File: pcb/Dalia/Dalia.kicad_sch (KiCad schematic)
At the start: 3 parts

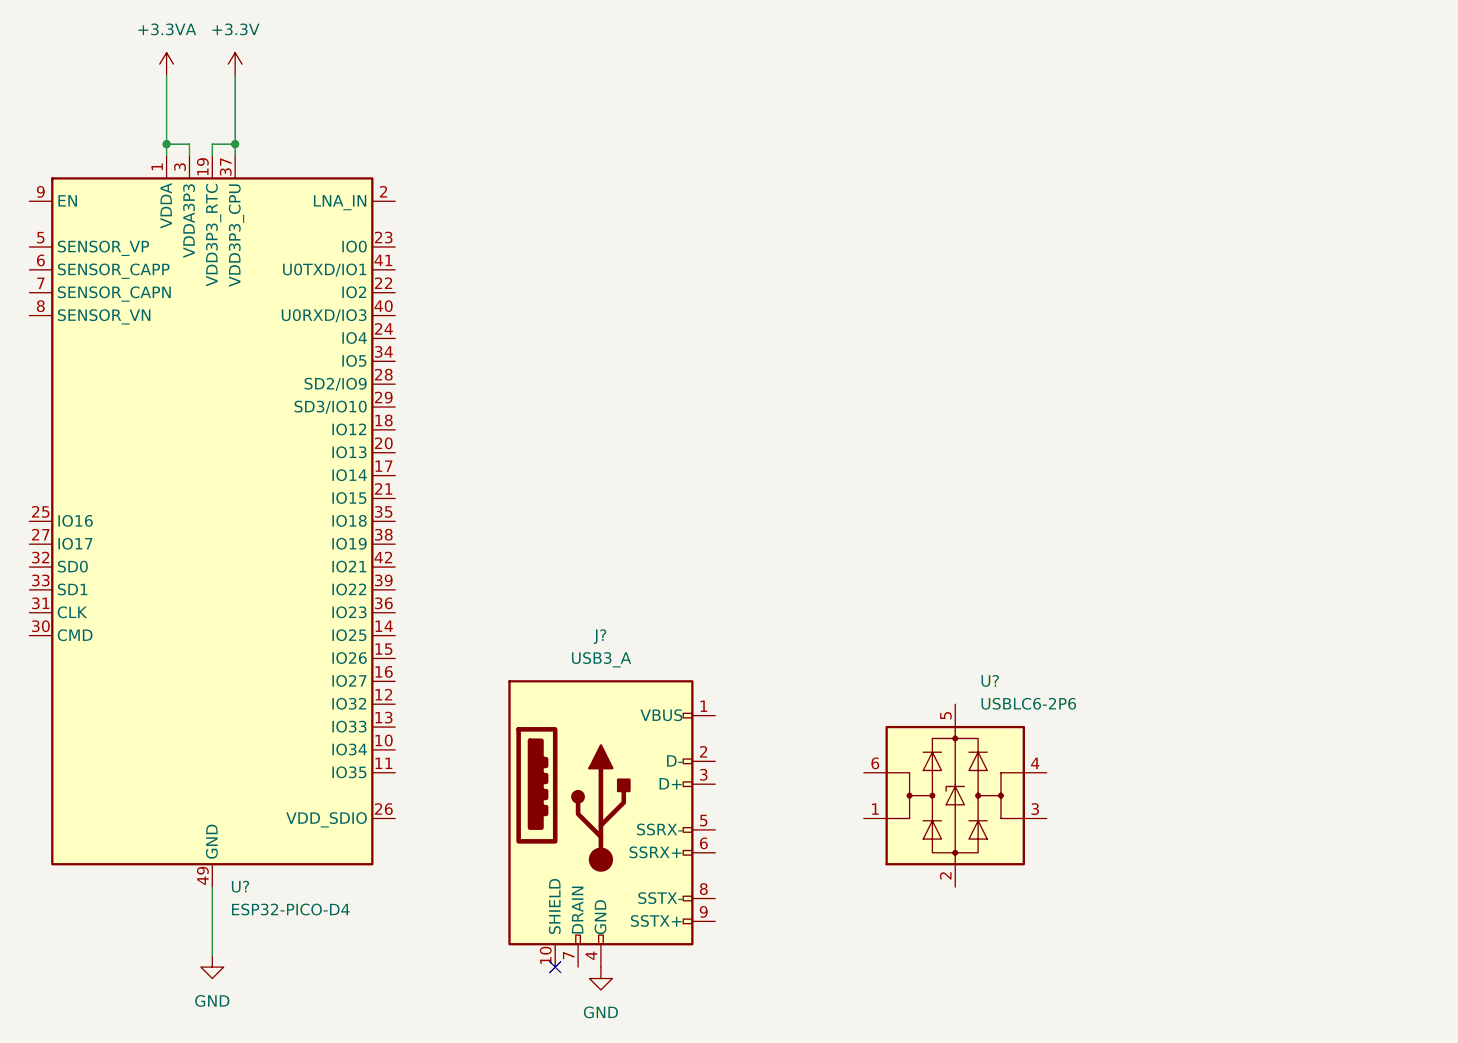
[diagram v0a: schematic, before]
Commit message: Changed PCB layout
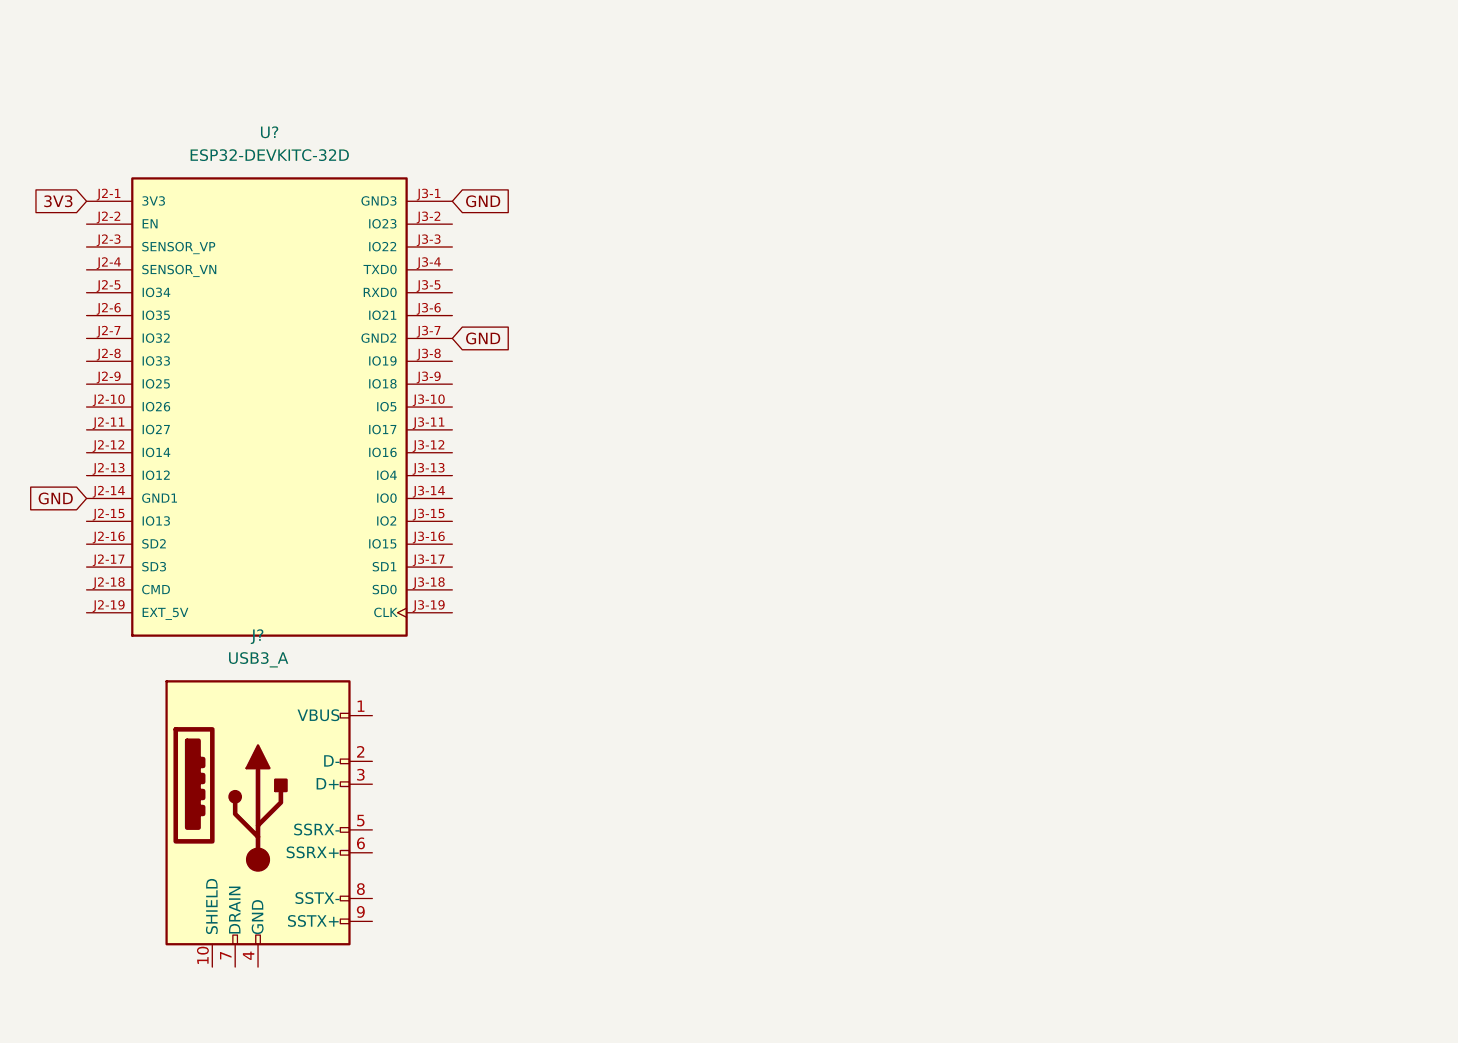
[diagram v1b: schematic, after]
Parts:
- removed U?: USBLC6-2P6, Package_TO_SOT_SMD:SOT-666, symbol Power_Protection:USBLC6-2P6
- removed U?: ESP32-PICO-D4, Package_DFN_QFN:QFN-48-1EP_7x7mm_P0.5mm_EP5.3x5.3mm, symbol RF_Module:ESP32-PICO-D4
- added U?: ESP32-DEVKITC-32D, MODULE_ESP32-DEVKITC-32D, symbol ESP32-DEVKITC-32D:ESP32-DEVKITC-32D
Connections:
- net GND: now also U?.J2-14 (GND1), U?.J3-1 (GND3), U?.J3-7 (GND2); no longer J?.4 (GND)
- new net 3V3: U?.J2-1 (3V3)
- no-connect marks 1 -> 0
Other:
- moved on the sheet: J?

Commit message: Updated PCB
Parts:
- removed J?: USB3_A, symbol Connector:USB3_A
- added J?: USB_B_Micro, symbol Connector:USB_B_Micro
- added U?: USBLC6-2SC6, Package_TO_SOT_SMD:SOT-23-6, symbol Power_Protection:USBLC6-2SC6
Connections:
- net GND: now also J?.5 (GND), U?.2 (GND)
- new net +5V: J?.1 (VBUS), U?.5 (VBUS)
- new net USB_CONN_D+: J?.3 (D+), U?.3 (I/O2)
- new net USB_CONN_D-: J?.2 (D-), U?.1 (I/O1)
- no-connect marks 0 -> 2
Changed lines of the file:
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@@
     (company "AndromedaHelix")
   )
+  (no_connect (at 190.5 130.81))
+  (no_connect (at 200.66 125.73))
+  (global_label "GND" (shape input) (at 193.04 130.81 270) (fields_autoplaced)
+    (effects (font (size 1.27 1.27)) (justify right))
+    (property "Intersheet References" "${INTERSHEET_REFS}" (id 0) (at 192.9606 137.0936 90)
+      (effects (font (size 1.27 1.27)) (justify right) hide)
+    )
+  )
   (global_label "GND" (shape input) (at 168.91 69.85 0) (fields_autoplaced)
     (effects (font (size 1.27 1.27)) (justify left))
@@
     )
   )
+  (global_label "USB_CONN_D-" (shape input) (at 200.66 123.19 0) (fields_autoplaced)
+    (effects (font (size 1.27 1.27)) (justify left))
+    (property "Intersheet References" "${INTERSHEET_REFS}" (id 0) (at 216.9221 123.1106 0)
+      (effects (font (size 1.27 1.27)) (justify left) hide)
+    )
+  )
   (global_label "GND" (shape input) (at 168.91 85.09 0) (fields_autoplaced)
     (effects (font (size 1.27 1.27)) (justify left))
@@
     )
   )
+  (global_label "USB_CONN_D-" (shape input) (at 240.03 123.19 180) (fields_autoplaced)
+    (effects (font (size 1.27 1.27)) (justify right))
+    (property "Intersheet References" "${INTERSHEET_REFS}" (id 0) (at 223.7679 123.2694 0)
+      (effects (font (size 1.27 1.27)) (justify right) hide)
+    )
+  )
   (global_label "GND" (shape input) (at 128.27 102.87 180) (fields_autoplaced)
     (effects (font (size 1.27 1.27)) (justify right))
@@
       (effects (font (size 1.27 1.27)) (justify right) hide)
     )
+  )
+  (global_label "GND" (shape input) (at 250.19 130.81 270) (fields_autoplaced)
+    (effects (font (size 1.27 1.27)) (justify right))
+    (property "Intersheet References" "${INTERSHEET_REFS}" (id 0) (at 250.1106 137.0936 90)
+      (effects (font (size 1.27 1.27)) (justify right) hide)
+    )
+  )
+  (global_label "USB_CONN_D+" (shape input) (at 260.35 123.19 0) (fields_autoplaced)
+    (effects (font (size 1.27 1.27)) (justify left))
+    (property "Intersheet References" "${INTERSHEET_REFS}" (id 0) (at 276.6121 123.1106 0)
+      (effects (font (size 1.27 1.27)) (justify left) hide)
+    )
+  )
+  (global_label "USB_CONN_D+" (shape input) (at 200.66 120.65 0) (fields_autoplaced)
+    (effects (font (size 1.27 1.27)) (justify left))
+    (property "Intersheet References" "${INTERSHEET_REFS}" (id 0) (at 216.9221 120.5706 0)
+      (effects (font (size 1.27 1.27)) (justify left) hide)
+    )
+  )
+  (symbol (lib_id "Power_Protection:USBLC6-2SC6") (at 250.19 120.65 0) (unit 1)
+    (in_bom yes) (on_board yes) (fields_autoplaced)
+    (property "Reference" "U?" (id 0) (at 252.9587 107.95 0)
+      (effects (font (size 1.27 1.27)) (justify left))
+    )
+    (property "Value" "USBLC6-2SC6" (id 1) (at 252.9587 110.49 0)
+      (effects (font (size 1.27 1.27)) (justify left))
+    )
+    (property "Footprint" "Package_TO_SOT_SMD:SOT-23-6" (id 2) (at 250.19 133.35 0)
+      (effects (font (size 1.27 1.27)) hide)
+    )
+    (property "Datasheet" "https://www.st.com/resource/en/datasheet/usblc6-2.pdf" (id 3) (at 255.27 111.76 0)
+      (effects (font (size 1.27 1.27)) hide)
+    )
+    (pin "1")
+    (pin "2")
+    (pin "3")
+    (pin "4")
+    (pin "5")
+    (pin "6")
   )
   (symbol (lib_id "ESP32-DEVKITC-32D:ESP32-DEVKITC-32D") (at 148.59 92.71 0) (unit 1)
@@
     (pin "J3-9")
   )
-  (symbol (lib_id "Connector:USB3_A") (at 147.32 137.16 0) (unit 1)
-    (in_bom yes) (on_board yes) (fields_autoplaced)
-    (property "Reference" "J?" (id 0) (at 147.32 118.11 0))
-    (property "Value" "USB3_A" (id 1) (at 147.32 120.65 0))
-    (property "Footprint" "" (id 2) (at 151.13 134.62 0)
-      (effects (font (size 1.27 1.27)) hide)
-    )
-    (property "Datasheet" "~" (id 3) (at 151.13 134.62 0)
-      (effects (font (size 1.27 1.27)) hide)
-    )
-    (pin "1")
-    (pin "10")
+  (symbol (lib_id "Connector:USB_B_Micro") (at 193.04 120.65 0) (unit 1)
+    (in_bom yes) (on_board yes) (fields_autoplaced)
+    (property "Reference" "J?" (id 0) (at 193.04 107.95 0))
+    (property "Value" "USB_B_Micro" (id 1) (at 193.04 110.49 0))
+    (property "Footprint" "" (id 2) (at 196.85 121.92 0)
+      (effects (font (size 1.27 1.27)) hide)
+    )
+    (property "Datasheet" "~" (id 3) (at 196.85 121.92 0)
+      (effects (font (size 1.27 1.27)) hide)
+    )
+    (pin "1")
     (pin "2")
     (pin "3")
@@
     (pin "5")
     (pin "6")
-    (pin "7")
-    (pin "8")
-    (pin "9")
+  )
+  (symbol (lib_id "power:+5V") (at 200.66 115.57 0) (unit 1)
+    (in_bom yes) (on_board yes) (fields_autoplaced)
+    (property "Reference" "#PWR?" (id 0) (at 200.66 119.38 0)
+      (effects (font (size 1.27 1.27)) hide)
+    )
+    (property "Value" "+5V" (id 1) (at 200.66 110.49 0))
+    (property "Footprint" "" (id 2) (at 200.66 115.57 0)
+      (effects (font (size 1.27 1.27)) hide)
+    )
+    (property "Datasheet" "" (id 3) (at 200.66 115.57 0)
+      (effects (font (size 1.27 1.27)) hide)
+    )
+    (pin "1")
+  )
+  (symbol (lib_id "power:+5V") (at 250.19 110.49 0) (unit 1)
+    (in_bom yes) (on_board yes) (fields_autoplaced)
+    (property "Reference" "#PWR?" (id 0) (at 250.19 114.3 0)
+      (effects (font (size 1.27 1.27)) hide)
+    )
+    (property "Value" "+5V" (id 1) (at 250.19 105.41 0))
+    (property "Footprint" "" (id 2) (at 250.19 110.49 0)
+      (effects (font (size 1.27 1.27)) hide)
+    )
+    (property "Datasheet" "" (id 3) (at 250.19 110.49 0)
+      (effects (font (size 1.27 1.27)) hide)
+    )
+    (pin "1")
   )
   (sheet_instances
@@
   )
   (symbol_instances
-    (path "/8f4e2a89-f072-458e-afb3-673b3d29090b"
-      (reference "J?") (unit 1) (value "USB3_A") (footprint "")
+    (path "/acbc059b-c5dd-4e78-9076-4d0d5dff753c"
+      (reference "#PWR?") (unit 1) (value "+5V") (footprint "")
+    )
+    (path "/f56ce442-d11b-40b3-8c54-dce5c48e1dbe"
+      (reference "#PWR?") (unit 1) (value "+5V") (footprint "")
+    )
+    (path "/78f58473-7315-4827-b173-aa781c6fb7e3"
+      (reference "J?") (unit 1) (value "USB_B_Micro") (footprint "")
+    )
+    (path "/38a38a2f-3588-41e0-966c-b7cba737b687"
+      (reference "U?") (unit 1) (value "USBLC6-2SC6") (footprint "Package_TO_SOT_SMD:SOT-23-6")
     )
     (path "/41af8376-181e-4c15-96fd-62e389a090fe"
